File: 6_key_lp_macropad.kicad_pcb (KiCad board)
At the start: 2 copper layers, 57.2 x 57.2 mm, 10 parts, among them SW1 Rotary_Encoder_Switch, SW2 SW_Push, U1 ProMicro

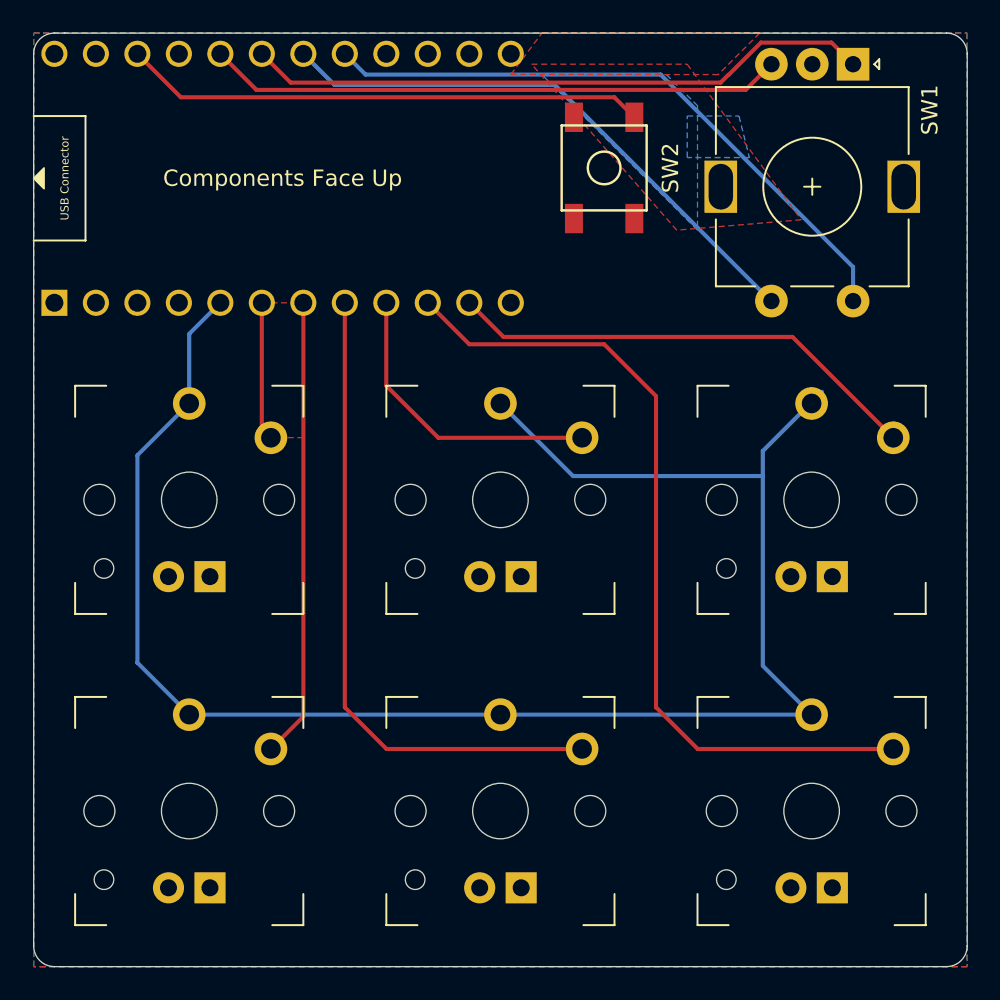
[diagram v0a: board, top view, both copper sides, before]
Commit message: Flipped MCU to allow for stronger USB connector
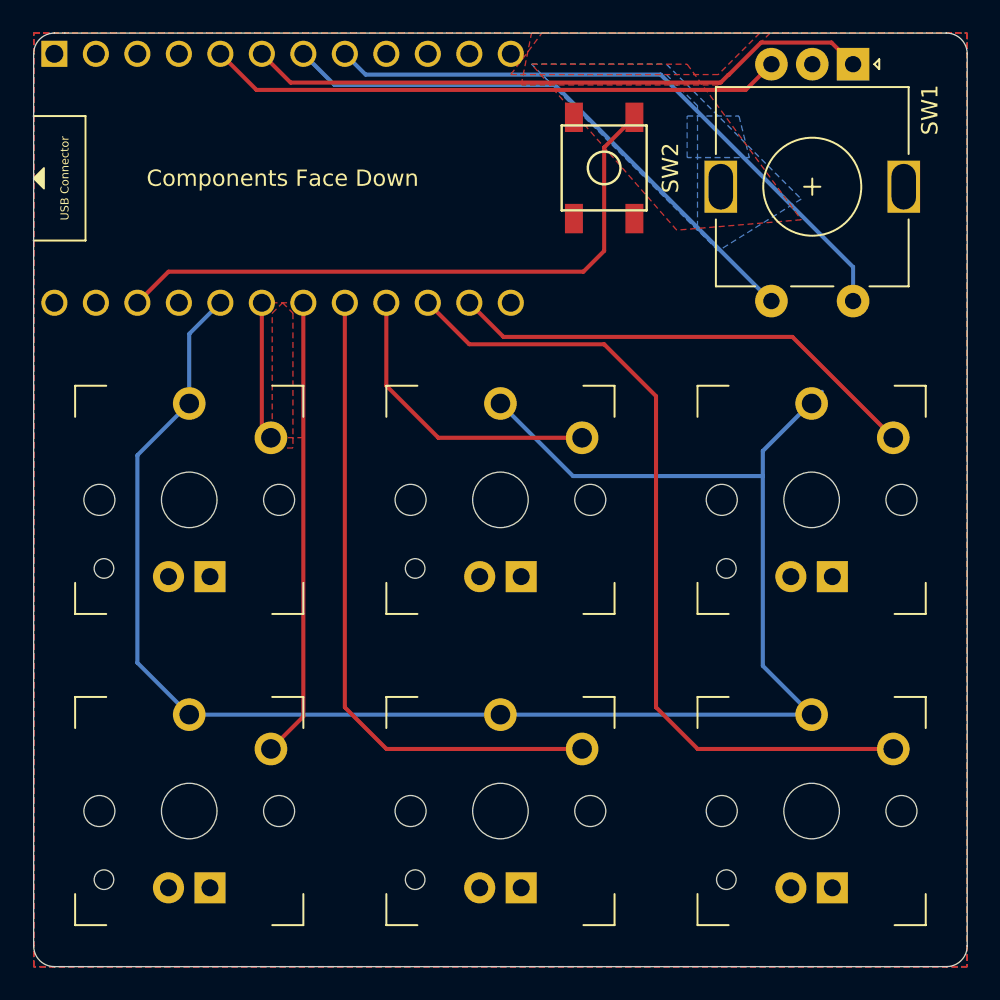
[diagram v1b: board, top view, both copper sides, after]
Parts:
- U1: moved to B.Cu
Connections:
- U1 pad 10: col5 -> Net-(U1-Pad10)
- U1 pad 11: col4 -> Net-(U1-Pad11)
- U1 pad 14: Net-(U1-Pad14) -> col4
- U1 pad 15: Net-(U1-Pad15) -> col5
- U1 pad 16: Net-(U1-Pad16) -> col2
- U1 pad 17: rot2 -> col3
- U1 pad 18: rot1 -> col1
- U1 pad 19: pinA -> col0
- U1 pad 20: pinB -> row0
- U1 pad 5: row0 -> pinB
- U1 pad 6: col0 -> pinA
- U1 pad 7: col1 -> rot1
- U1 pad 8: col3 -> rot2
- U1 pad 9: col2 -> Net-(U1-Pad9)
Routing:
- net reset: track 32.0 -> 38.8 mm
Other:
- board text added: "Components Face Down"
- board text removed: "Components Face Up"

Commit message: Fixed Ground Fills and Added Gerbers
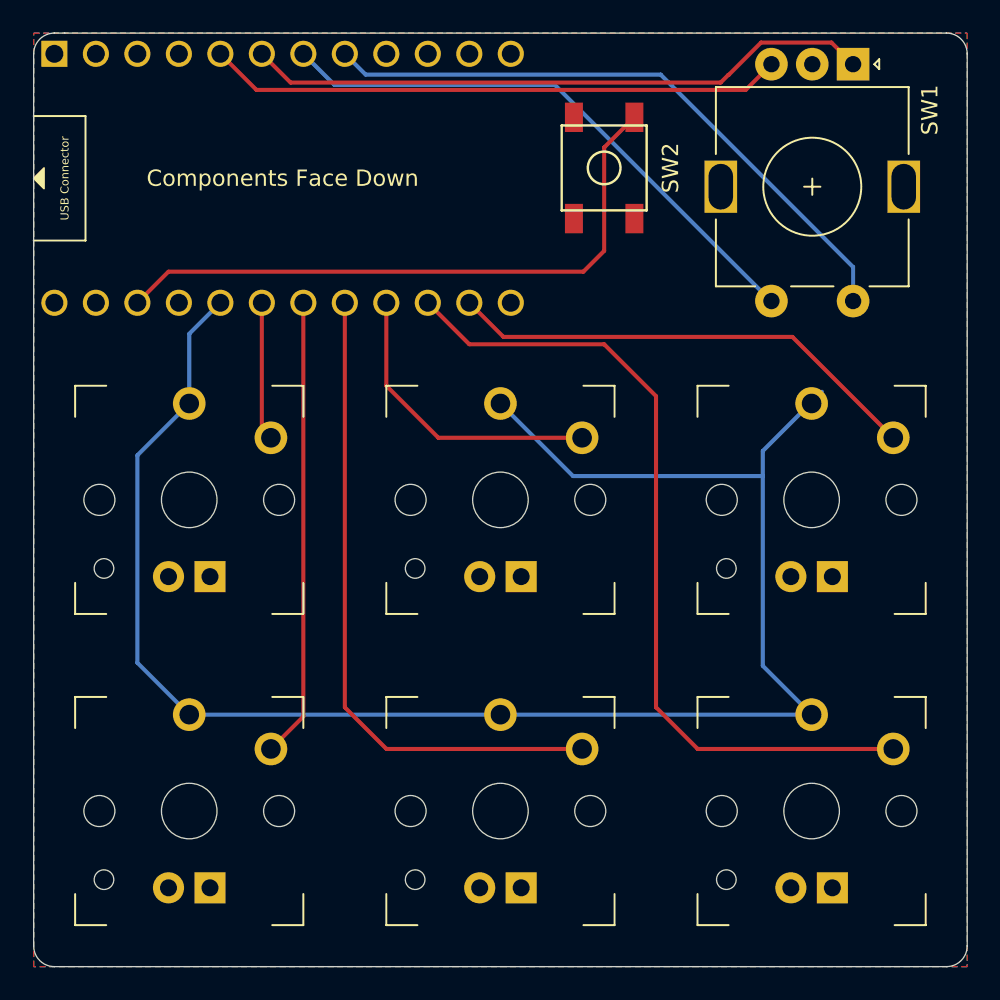
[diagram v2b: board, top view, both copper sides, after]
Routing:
- removed copper zone on B.Cu, net (none)
- removed copper zone on F.Cu, net (none)

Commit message: Corrected for direct pin assignment
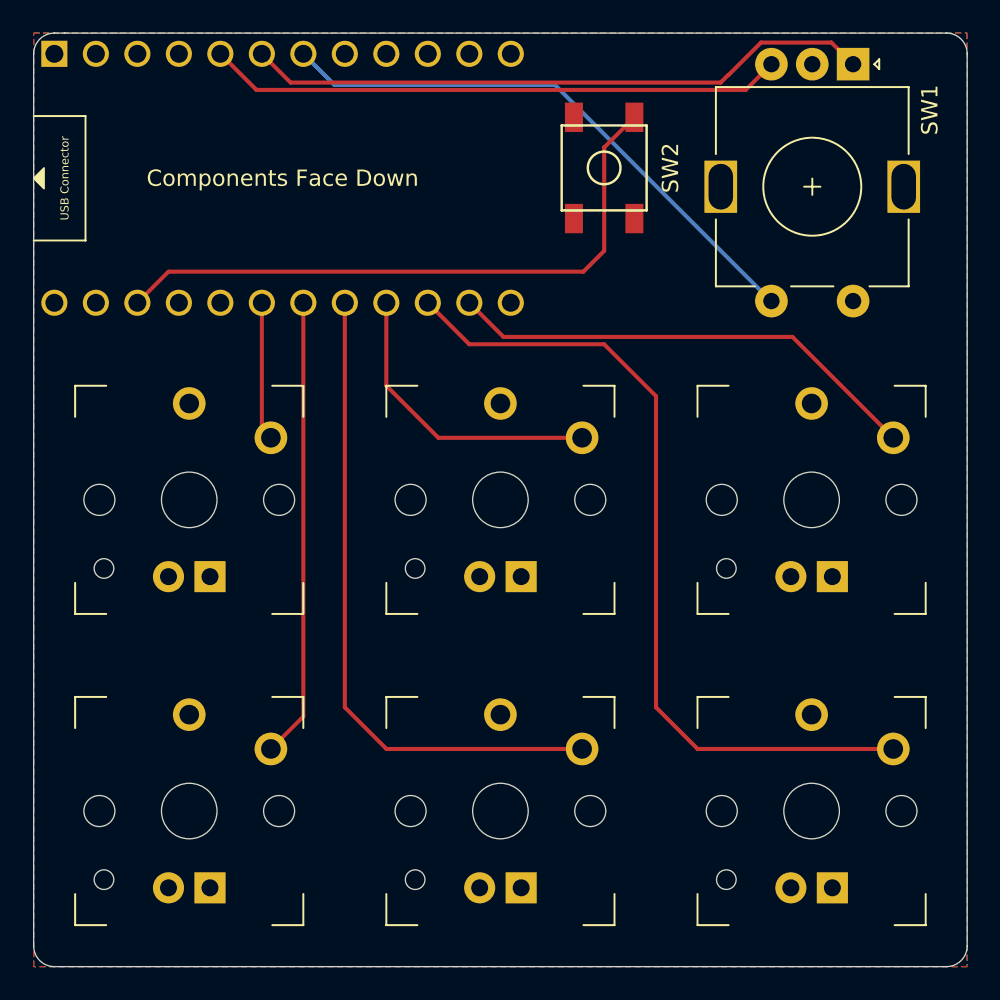
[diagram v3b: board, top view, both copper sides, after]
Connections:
- MX1 pad 2: row0 -> GND
- MX2 pad 2: row0 -> GND
- MX3 pad 2: row0 -> GND
- MX4 pad 2: row0 -> GND
- MX5 pad 2: row0 -> GND
- MX6 pad 2: row0 -> GND
- SW1 pad S2: rot2 -> GND
- U1 pad 20: row0 -> Net-(U1-Pad20)
- U1 pad 8: rot2 -> Net-(U1-Pad8)
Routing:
- net row0: track 107.1 -> 0.00 mm
- net rot2: track 38.6 -> 0.00 mm
